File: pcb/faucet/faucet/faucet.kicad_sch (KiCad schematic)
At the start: 7 parts, among them J1 Conn_01x04_Female, J2 Jack-DC, P1 Conn_WallPlug

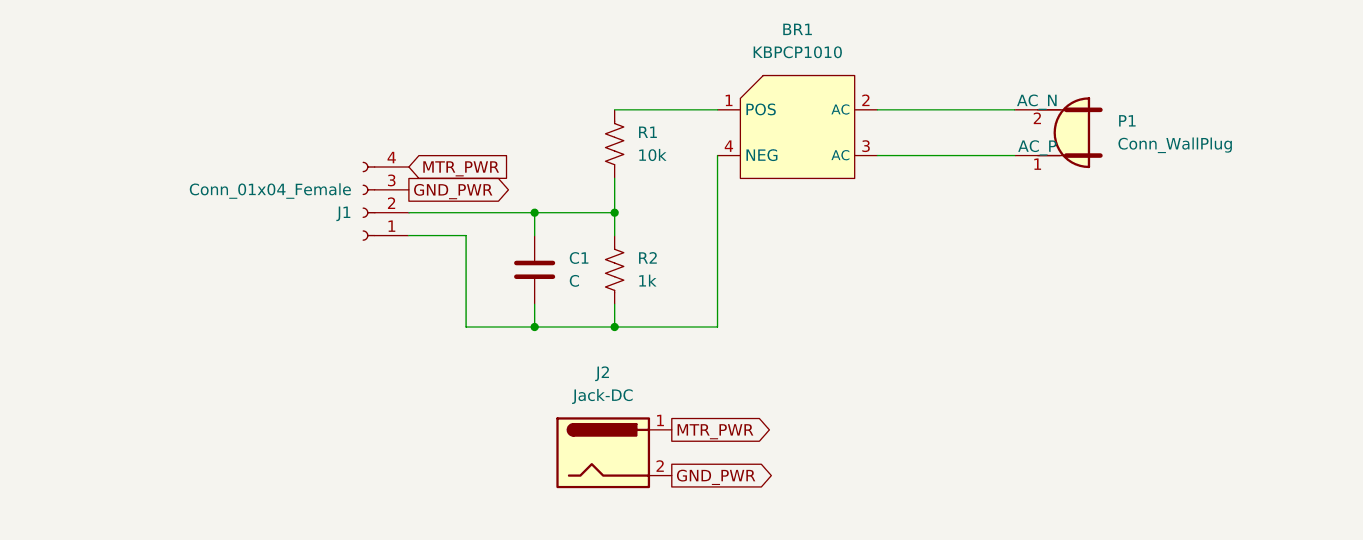
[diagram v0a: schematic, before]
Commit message: Finalize R and C values, add branding, ordered this board
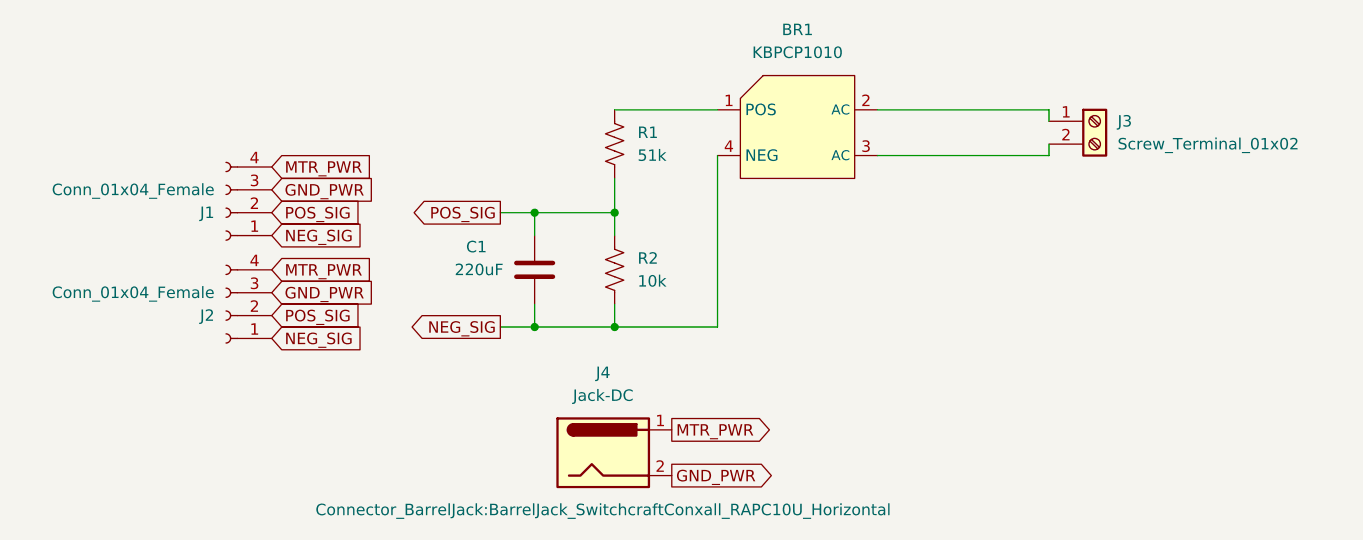
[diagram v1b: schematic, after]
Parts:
- removed P1: Conn_WallPlug, Connector_AMASS:AMASS_XT60-M_1x02_P7.20mm_Vertical, symbol Connector:Conn_WallPlug
- added J2: Conn_01x04_Female, Connector_PinSocket_2.54mm:PinSocket_1x04_P2.54mm_Vertical, symbol Connector:Conn_01x04_Female
- added J3: Screw_Terminal_01x02, TerminalBlock:TerminalBlock_Altech_AK300-2_P5.00mm, symbol Connector:Screw_Terminal_01x02
- C1: value C -> 220uF
- R1: value 10k -> 51k
- R2: value 1k -> 10k
- renumbered J2 to J4
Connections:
- net GND_PWR: now also J2.3 (Pin_3)
- net MTR_PWR: now also J2.4 (Pin_4)
- net at BR1.3 (AC): now also J3.2 (Pin_2)
- net at BR1.2 (AC): now also J3.1 (Pin_1)
- net NEG_SIG: now reaches BR1.4 (NEG), C1.2, J1.1 (Pin_1), R2.2
- net NEG_SIG: now also J2.1 (Pin_1)
- net POS_SIG: now reaches C1.1, J1.2 (Pin_2), R1.2, R2.1
- net POS_SIG: now also J2.2 (Pin_2)
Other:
- moved on the sheet: J1
